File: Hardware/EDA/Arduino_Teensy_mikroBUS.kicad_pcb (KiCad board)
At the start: 4 copper layers, 45.7 x 69.8 mm, 30 parts, among them J1 HEADER_F_2.54MM_1R8P_ST_AU_PTH, J2 HEADER_F_2.54MM_1R8P_ST_AU_PTH, J3 HEADER_F_2.54MM_1R14P_ST_AU_P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, J4 HEADER_F_2.54MM_1R14P_ST_AU_P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, J5 Molex_0475710001, M1 FID, M2 FID, M3 FID, P1 HEADER_M_2.54MM_1R4P_ST_AU_PTH, P2 HEADER_M_2.54MM_1R4P_ST_AU_PTH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

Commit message: Final changes prior to gerber verification.
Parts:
- moved M1 2.54 mm to (99.1, 88.9)
- moved M2 2.54 mm to (99.1, 44.5)
- moved M3 2.54 mm to (61.0, 44.5)
- moved LK1 1.52 mm to (62.7, 37.6)
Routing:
- net mikroBUS_RST: track 4.37 -> 5.89 mm
- net D3: track 60.5 -> 61.1 mm
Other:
- board text added: "Corrections made: Add silkscreen pin names to mikroBUS connector Verified flash functionality through testing Corrected pin numbering of 2xAA battery holder footprint to match schematic decal Corrected pin numbering of 1x9V battery holder footprint to match schematic decal Re-layed out 2xAA battery traces Re-layed out 1x9V battery traces Added silkscreen pin names to Grove connector Add silkscree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"
- board text added: "Corrections needed:"
- board text removed: "Corrections made:"
- board text removed: "Corrections needed: RTC needs crystal and caps Add silkscreen pin names to mikroBUS connector Check FL127 footprint against Winbond footprint Add level shifter for microSD socket? Corrected pin numbering of 2xAA battery holder footprint to match schematic decal Corrected pin numbering of 1x9V battery holder footprint to match schematic decal Re-layed out 2xAA battery traces Re-layed out 1x9V batt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"
- board text removed: "RAW"
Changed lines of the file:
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@@
-(kicad_pcb (version 4) (host pcbnew 4.0.6)
+(kicad_pcb (version 4) (host pcbnew 4.0.4-stable)
   (general
     (links 80)
     (no_connects 0)
-    (area 41.374287 25.24 113.565715 113.190001)
+    (area 41.374287 25.24 211.371426 113.190001)
     (thickness 1.6)
-    (drawings 31)
+    (drawings 57)
     (tracks 271)
     (zones 0)
@@
       (effects (font (size 1.016 1.016) (thickness 0.1524)) (justify mirror))
     )
-    (fp_line (start 24.892 -7.62) (end 25.908 -7.62) (layer B.SilkS) (width 0.127))
-    (fp_circle (center 25.4 -7.62) (end 26.416 -7.62) (layer B.SilkS) (width 0.127))
-    (fp_line (start 25.4 -7.112) (end 25.4 -8.128) (layer B.SilkS) (width 0.127))
-    (fp_line (start 25.4 8.128) (end 25.4 7.112) (layer B.SilkS) (width 0.127))
-    (fp_circle (center 25.4 7.62) (end 26.416 7.62) (layer B.SilkS) (width 0.127))
+    (fp_line (start 27.432 -4.826) (end 28.448 -4.826) (layer B.SilkS) (width 0.127))
+    (fp_circle (center 27.94 -4.826) (end 28.956 -4.826) (layer B.SilkS) (width 0.127))
+    (fp_line (start 27.94 -4.318) (end 27.94 -5.334) (layer B.SilkS) (width 0.127))
+    (fp_line (start 27.94 5.334) (end 27.94 4.318) (layer B.SilkS) (width 0.127))
+    (fp_circle (center 27.94 4.826) (end 28.956 4.826) (layer B.SilkS) (width 0.127))
     (fp_line (start -30.48 16.51) (end -30.48 -16.51) (layer B.SilkS) (width 0.127))
     (fp_line (start -30.48 -16.51) (end 30.48 -16.51) (layer B.SilkS) (width 0.127))
@@
     (at 91.44 43.18 270)
     (tags Header)
-    (fp_text reference J2 (at -8.89 -2.54 360) (layer F.SilkS)
+    (fp_text reference J2 (at 11.176 0 360) (layer F.SilkS)
       (effects (font (size 1.016 1.016) (thickness 0.1524)))
     )
@@
     (at 68.58 43.18 270)
     (tags Header)
-    (fp_text reference J1 (at -8.89 2.54 360) (layer F.SilkS)
+    (fp_text reference J1 (at 11.176 0 360) (layer F.SilkS)
       (effects (font (size 1.016 1.016) (thickness 0.1524)))
     )
@@
   )
   (module Passive:SOLDER_LINK_NO (layer F.Cu)
-    (at 64.262 37.592 180)
+    (at 62.738 37.592 180)
     (fp_text reference LK1 (at 1.524 0 450) (layer F.SilkS)
       (effects (font (size 1.016 1.016) (thickness 0.1524)))
@@
   )
   (module FIDUCIAL:FIDUCIAL locked (layer F.Cu)
-    (at 96.52 88.9)
+    (at 99.06 88.9)
     (fp_text reference M1 (at 0 -1.778) (layer F.SilkS) hide
       (effects (font (size 0.4572 0.508) (thickness 0.1016)))
@@
   )
   (module FIDUCIAL:FIDUCIAL locked (layer F.Cu)
-    (at 96.52 44.45)
+    (at 99.06 44.45)
     (fp_text reference M2 (at 0 -1.778) (layer F.SilkS) hide
       (effects (font (size 0.4572 0.508) (thickness 0.1016)))
@@
   )
   (module FIDUCIAL:FIDUCIAL locked (layer F.Cu)
-    (at 63.5 44.45)
+    (at 60.96 44.45)
     (fp_text reference M3 (at 0 -1.778) (layer F.SilkS) hide
       (effects (font (size 0.4572 0.508) (thickness 0.1016)))
@@
     )
   )
-  (gr_text GND (at 90.17 96.52) (layer F.SilkS)
-    (effects (font (size 1.016 1.016) (thickness 0.2032)))
-  )
-  (gr_text VIN (at 69.85 96.52) (layer F.SilkS)
+  (gr_text GND (at 90.932 96.52) (layer F.SilkS)
+    (effects (font (size 1.016 1.016) (thickness 0.2032)))
+  )
+  (gr_text VIN (at 69.342 96.52) (layer F.SilkS)
     (effects (font (size 1.016 1.016) (thickness 0.2032)))
   )
@@
     (effects (font (size 1.016 1.016) (thickness 0.2032)))
   )
-  (gr_text TXD (at 90.678 87.63) (layer F.SilkS)
-    (effects (font (size 1.016 1.016) (thickness 0.2032)))
-  )
-  (gr_text RAW (at 69.342 87.63) (layer F.SilkS)
-    (effects (font (size 1.016 1.016) (thickness 0.2032)))
-  )
   (gr_text SCL (at 100.15 70.4) (layer F.SilkS)
     (effects (font (size 1.016 1.016) (thickness 0.2032)))
@@
     (effects (font (size 1.016 1.016) (thickness 0.2032)))
   )
-  (gr_text "Corrections made:" (at 114.3 64.77) (layer Cmts.User)
+  (gr_text "Corrections made:\nAdd silkscreen pin names to mikroBUS connector\nVerified flash functionality through testing\nCorrected pin numbering of 2xAA battery holder footprint to match schematic decal\nCorrected pin numbering of 1x9V battery holder footprint to match schematic decal\nRe-layed out 2xAA battery traces\nRe-layed out 1x9V battery traces\nAdded silkscreen pin names to Grove connector\nAdd silkscreen orientation to Arduino socket" (at 114.3 64.77) (layer Cmts.User)
     (effects (font (size 1.5 1.5) (thickness 0.3)) (justify left))
   )
-  (gr_text "Corrections needed:\nRTC needs crystal and caps\nAdd silkscreen pin names to mikroBUS connector\nCheck FL127 footprint against Winbond footprint\nAdd level shifter for microSD socket?\nCorrected pin numbering of 2xAA battery holder footprint to match schematic decal\nCorrected pin numbering of 1x9V battery holder footprint to match schematic decal\nRe-layed out 2xAA battery traces\nRe-layed out 1x9V battery traces\nAdded silkscreen pin names to Grove connector\nAdd silkscreen orientation to Arduino socket" (at 114.3 44.45) (layer Cmts.User)
+  (gr_text "Corrections needed:\n" (at 114.3 44.45) (layer Cmts.User)
     (effects (font (size 1.5 1.5) (thickness 0.3)) (justify left))
   )
@@
   (segment (start 87.884 60.452) (end 89.408 61.976) (width 0.1524) (layer B.Cu) (net 5))
   (segment (start 87.884 59.182) (end 87.884 60.452) (width 0.1524) (layer B.Cu) (net 5))
-  (segment (start 68.58 36.83) (end 64.389 36.83) (width 0.1524) (layer F.Cu) (net 6))
-  (segment (start 64.389 36.83) (end 64.262 36.957) (width 0.1524) (layer F.Cu) (net 6))
+  (segment (start 68.58 36.83) (end 62.865 36.83) (width 0.1524) (layer F.Cu) (net 6))
+  (segment (start 62.865 36.83) (end 62.738 36.957) (width 0.1524) (layer F.Cu) (net 6))
   (segment (start 68.58 34.29) (end 66.04 36.83) (width 0.1524) (layer B.Cu) (net 7))
   (segment (start 70.866 64.516) (end 72.39 66.04) (width 0.1524) (layer B.Cu) (net 7))
@@
   (segment (start 90.932 55.626) (end 94.742 51.816) (width 0.1524) (layer F.Cu) (net 16))
   (segment (start 93.726 61.976) (end 93.726 61.976) (width 0.1524) (layer F.Cu) (net 16))
-  (segment (start 64.262 38.227) (end 64.262 41.402) (width 0.1524) (layer F.Cu) (net 17))
+  (segment (start 62.738 38.227) (end 62.738 39.878) (width 0.1524) (layer F.Cu) (net 17))
+  (segment (start 66.04 43.18) (end 66.04 52.578) (width 0.1524) (layer F.Cu) (net 17))
+  (segment (start 66.04 52.578) (end 74.676 61.214) (width 0.1524) (layer F.Cu) (net 17))
+  (segment (start 74.676 61.214) (end 74.676 64.008) (width 0.1524) (layer F.Cu) (net 17))
+  (segment (start 74.676 64.008) (end 76.708 66.04) (width 0.1524) (layer F.Cu) (net 17))
+  (via (at 76.708 66.04) (size 0.4572) (drill 0.3048) (layers F.Cu B.Cu) (net 17))
+  (segment (start 76.708 66.04) (end 82.296 71.628) (width 0.1524) (layer B.Cu) (net 17))
+  (segment (start 82.296 71.628) (end 82.296 85.598) (width 0.1524) (layer B.Cu) (net 17))
+  (segment (start 82.296 85.598) (end 83.058 86.36) (width 0.1524) (layer B.Cu) (net 17))
+  (via (at 83.058 86.36) (size 0.4572) (drill 0.3048) (layers F.Cu B.Cu) (net 17))
   (segment (start 83.058 86.36) (end 87.63 86.36) (width 0.1524) (layer F.Cu) (net 17))
-  (via (at 83.058 86.36) (size 0.4572) (drill 0.3048) (layers F.Cu B.Cu) (net 17))
-  (segment (start 82.296 85.598) (end 83.058 86.36) (width 0.1524) (layer B.Cu) (net 17))
-  (segment (start 82.296 71.628) (end 82.296 85.598) (width 0.1524) (layer B.Cu) (net 17))
-  (segment (start 76.708 66.04) (end 82.296 71.628) (width 0.1524) (layer B.Cu) (net 17))
-  (via (at 76.708 66.04) (size 0.4572) (drill 0.3048) (layers F.Cu B.Cu) (net 17))
-  (segment (start 74.676 64.008) (end 76.708 66.04) (width 0.1524) (layer F.Cu) (net 17))
-  (segment (start 74.676 61.214) (end 74.676 64.008) (width 0.1524) (layer F.Cu) (net 17))
-  (segment (start 66.04 52.578) (end 74.676 61.214) (width 0.1524) (layer F.Cu) (net 17))
-  (segment (start 66.04 43.18) (end 66.04 52.578) (width 0.1524) (layer F.Cu) (net 17))
-  (segment (start 64.262 41.402) (end 66.04 43.18) (width 0.1524) (layer F.Cu) (net 17))
+  (segment (start 62.738 39.878) (end 66.04 43.18) (width 0.1524) (layer F.Cu) (net 17))
   (segment (start 94.488 81.28) (end 90.678 85.09) (width 0.1524) (layer B.Cu) (net 18))
   (segment (start 87.63 91.44) (end 90.678 88.392) (width 0.1524) (layer B.Cu) (net 18))

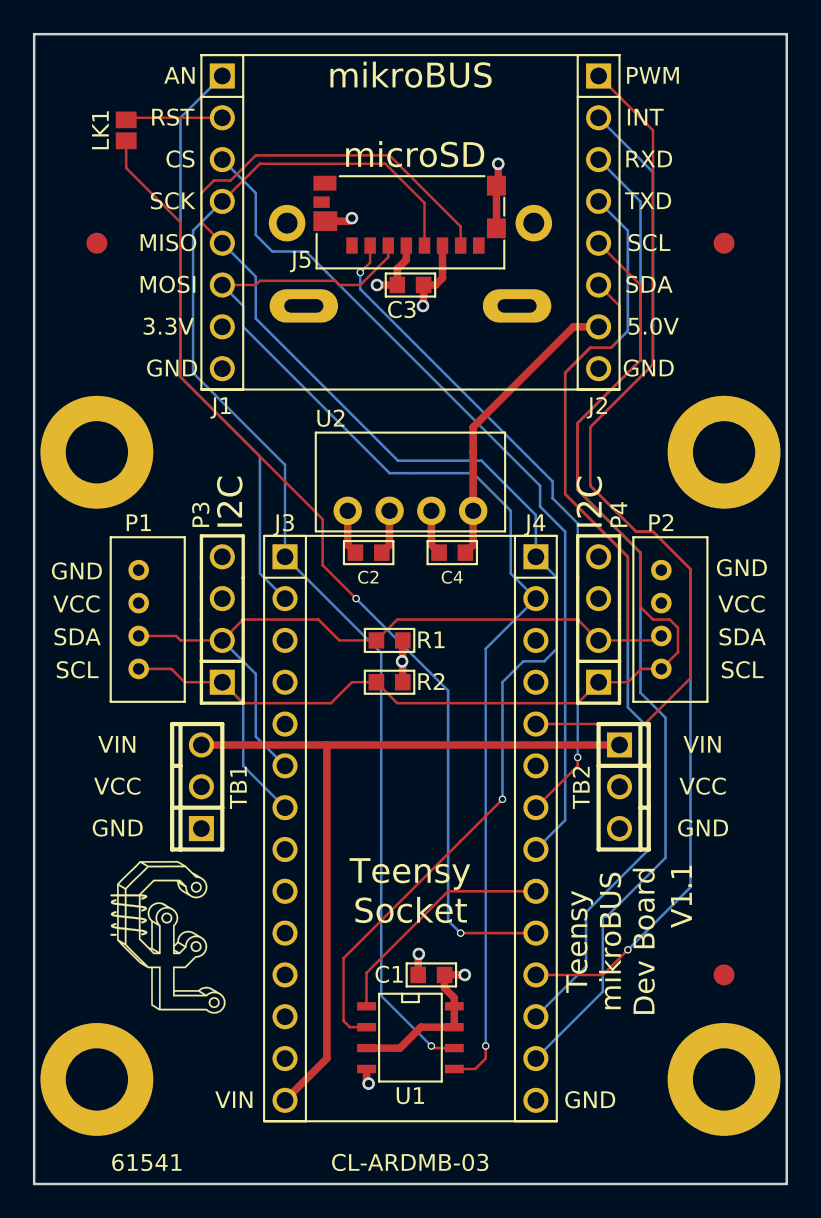
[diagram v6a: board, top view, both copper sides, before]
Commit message: Moved traces near MH2 to clean up layout. Regenerated Gerbers - need to be verified. Updated date in PCB title block. Regenerated PDF schematic.
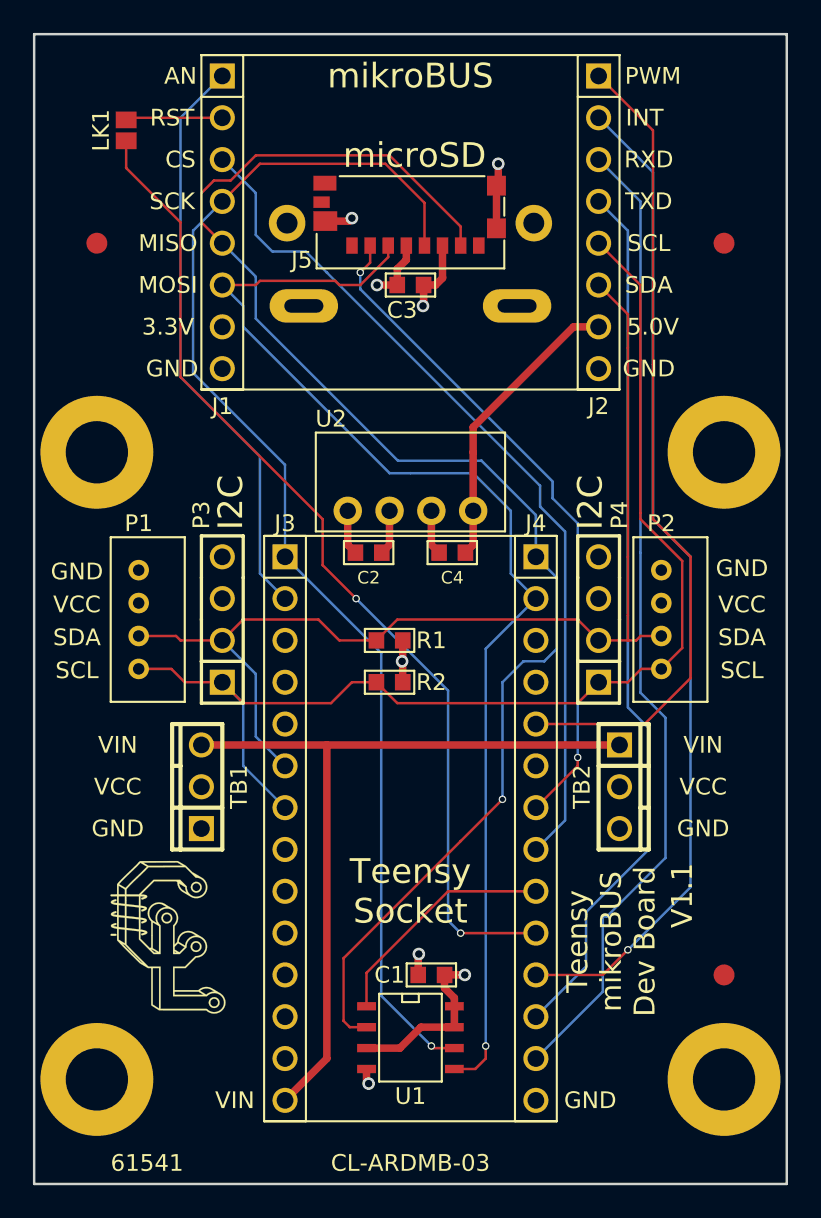
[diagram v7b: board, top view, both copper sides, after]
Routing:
- net TX1: track 57.5 -> 53.6 mm
- net D8: track 53.2 -> 49.4 mm
- net D2: track 64.4 -> 60.7 mm
- net SCL: track 75.8 -> 72.2 mm
- net SDA: track 69.1 -> 65.6 mm
- net RX1: track 62.9 -> 59.7 mm

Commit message: Removed change comments from PCB file.
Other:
- board text removed: "Corrections made: Add silkscreen pin names to mikroBUS connector Verified flash functionality through testing Corrected pin numbering of 2xAA battery holder footprint to match schematic decal Corrected pin numbering of 1x9V battery holder footprint to match schematic decal Re-layed out 2xAA battery traces Re-layed out 1x9V battery traces Added silkscreen pin names to Grove connector Add silkscree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"
- board text removed: "Corrections needed:"
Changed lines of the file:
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@@
     (links 80)
     (no_connects 0)
-    (area 57.074999 31.674999 102.945001 101.675001)
+    (area 41.374287 25.24 113.565715 113.190001)
     (thickness 1.6)
-    (drawings 57)
+    (drawings 55)
     (tracks 250)
     (zones 0)
@@
     (effects (font (size 1.016 1.016) (thickness 0.2032)))
   )
-  (gr_text "Corrections made:\nAdd silkscreen pin names to mikroBUS connector\nVerified flash functionality through testing\nCorrected pin numbering of 2xAA battery holder footprint to match schematic decal\nCorrected pin numbering of 1x9V battery holder footprint to match schematic decal\nRe-layed out 2xAA battery traces\nRe-layed out 1x9V battery traces\nAdded silkscreen pin names to Grove connector\nAdd silkscreen orientation to Arduino socket" (at 114.3 64.77) (layer Cmts.User)
-    (effects (font (size 1.5 1.5) (thickness 0.3)) (justify left))
-  )
-  (gr_text "Corrections needed:\n" (at 114.3 44.45) (layer Cmts.User)
-    (effects (font (size 1.5 1.5) (thickness 0.3)) (justify left))
-  )
   (dimension 41.91 (width 0.3) (layer Dwgs.User)
